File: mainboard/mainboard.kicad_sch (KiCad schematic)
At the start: 54 parts, among them J1 Servo, J2 ADC Pins, J3 USB Data, J4 Button Interface, J5 Power, J6 Release Button, J7 GPIO Pins, Q1 BSS138, SW1 SW_Push, U1 RP2040, U2 W25Q128JVS, U3 RV-3028-C7, U4 ITR9608-F, Y1 Crystal_ABM8

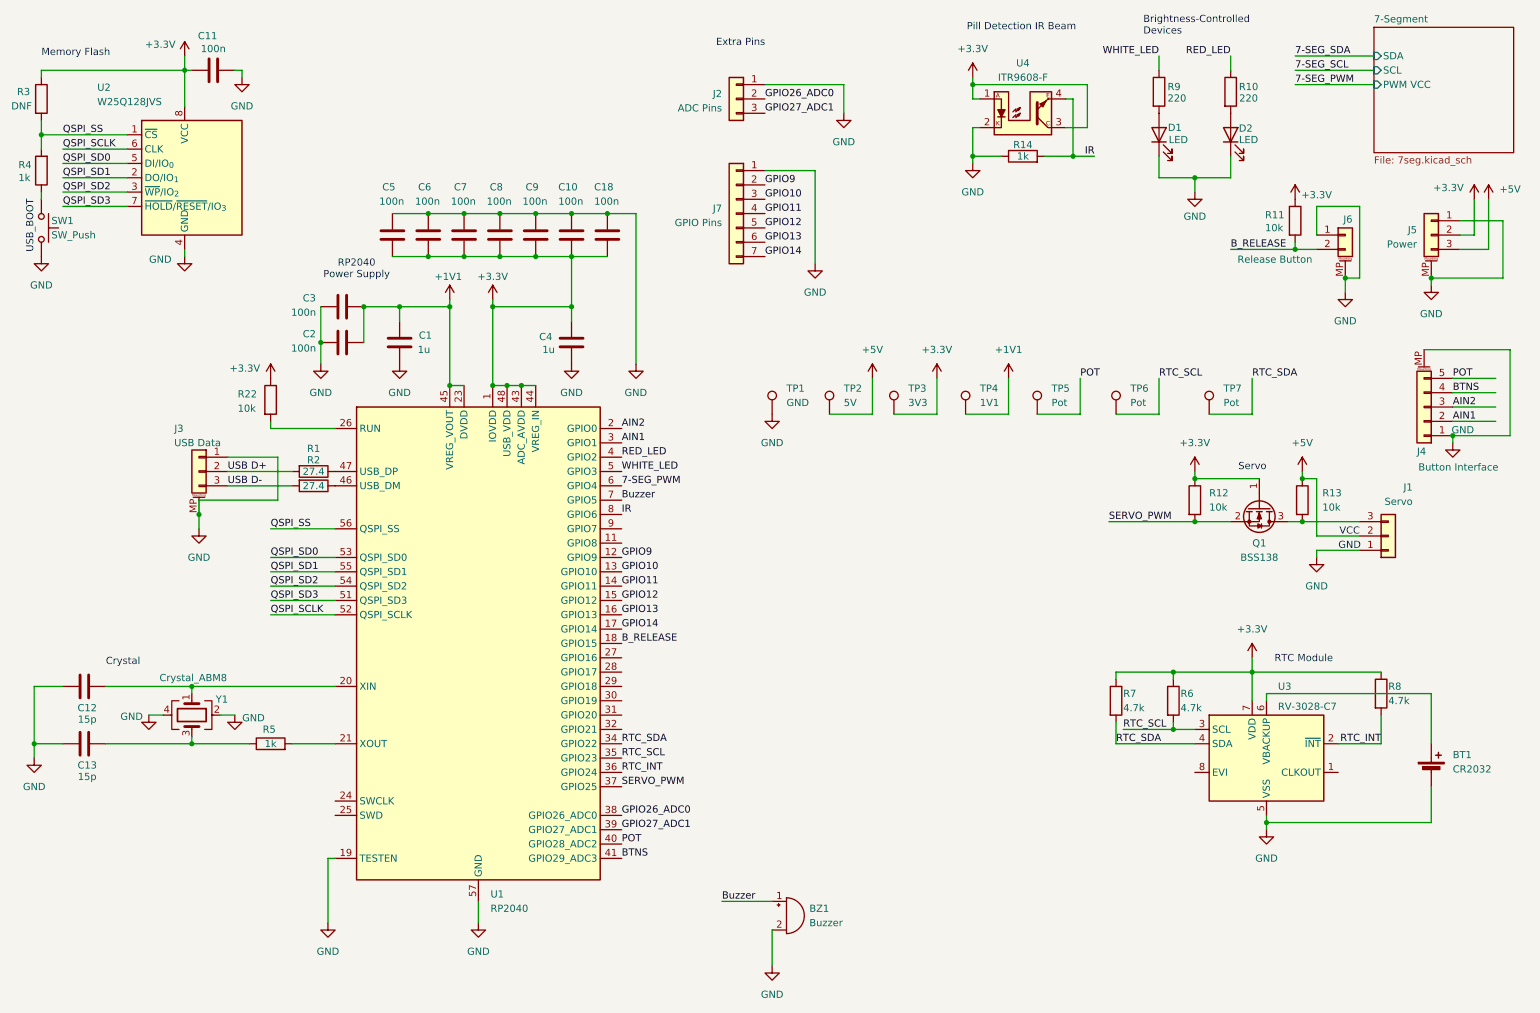
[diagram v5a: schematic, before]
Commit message: Replaced buzzer with connector, consolidated some connectors, rerouted traces.
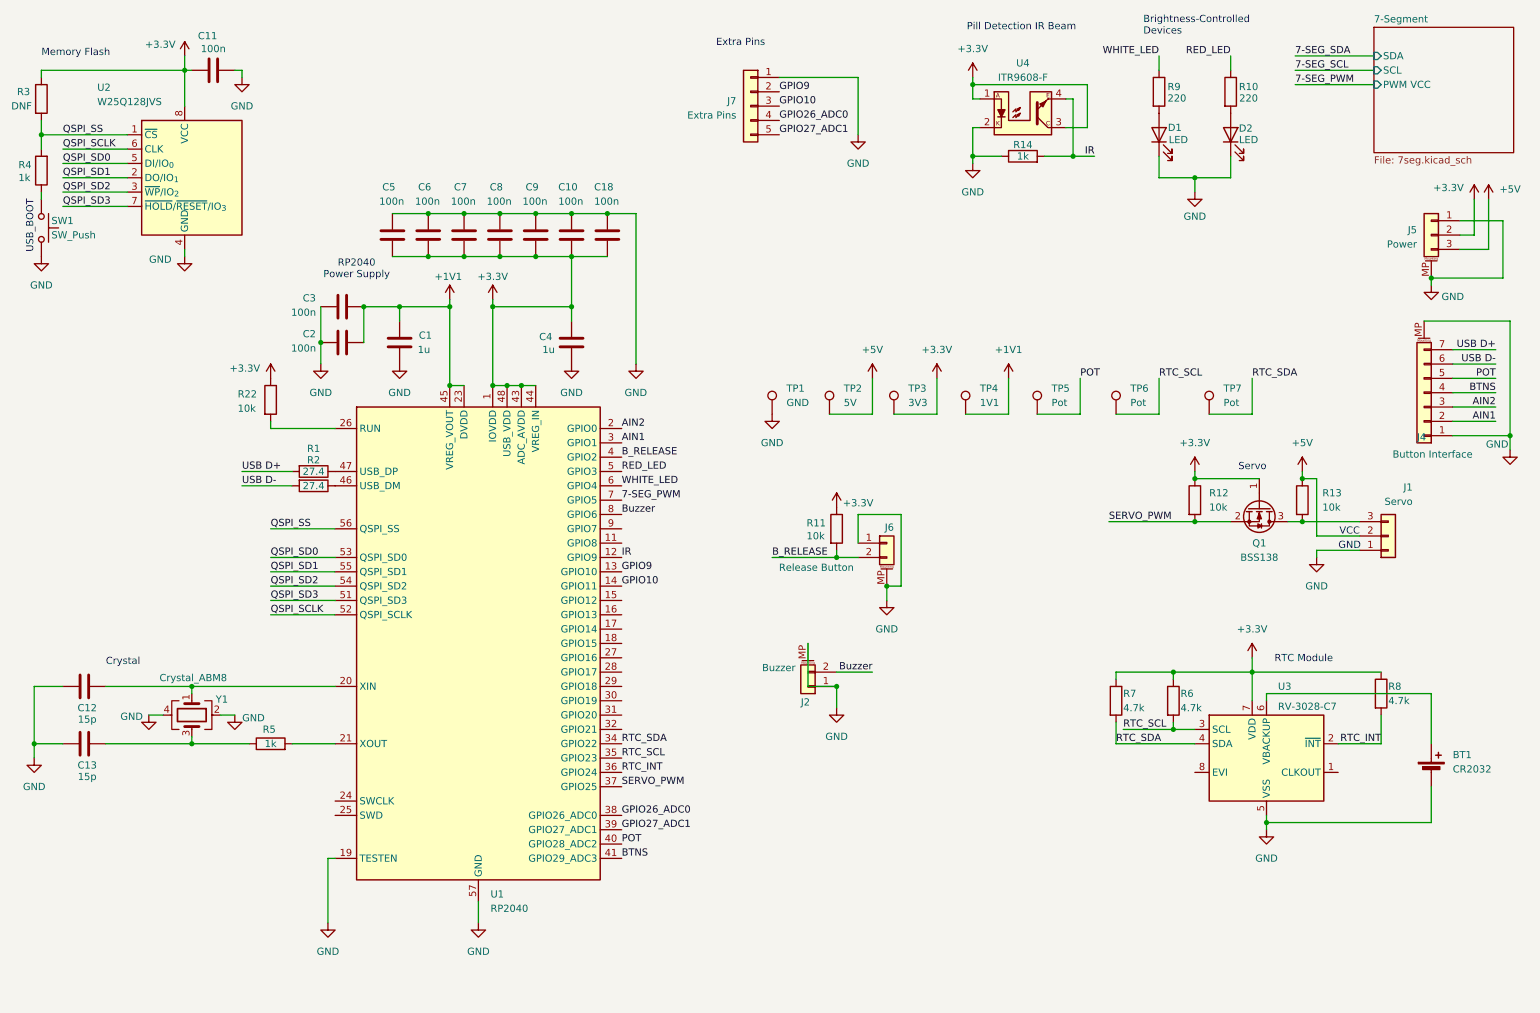
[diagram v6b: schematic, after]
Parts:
- removed BZ1: Buzzer, Buzzer_Beeper:Buzzer_12x9.5RM7.6, symbol Device:Buzzer
- removed J2: ADC Pins, Connector_PinHeader_2.54mm:PinHeader_1x03_P2.54mm_Vertical, symbol Connector_Generic:Conn_01x03
- removed J3: USB Data, Connector_Molex:Molex_CLIK-Mate_505405-0370_1x03-1MP_P1.50mm_Vertical, symbol Connector_Generic_MountingPin:Conn_01x03_MountingPin
- added J2: Buzzer, Connector_Molex:Molex_CLIK-Mate_505405-0270_1x02-1MP_P1.50mm_Vertical, symbol Connector_Generic_MountingPin:Conn_01x02_MountingPin
- D1, D2: footprint LED_THT:LED_D3.0mm -> LED_SMD:LED_1206_3216Metric
- J4: footprint Connector_Molex:Molex_CLIK-Mate_505405-0570_1x05-1MP_P1.50mm_Vertical -> Connector_Molex:Molex_CLIK-Mate_505405-0770_1x07-1MP_P1.50mm_Vertical; symbol Connector_Generic_MountingPin:Conn_01x05_MountingPin -> Connector_Generic_MountingPin:Conn_01x07_MountingPin
- J7: value GPIO Pins -> Extra Pins; footprint Connector_PinHeader_2.54mm:PinHeader_1x07_P2.54mm_Vertical -> Connector_PinHeader_2.54mm:PinHeader_1x05_P2.54mm_Vertical; symbol Connector_Generic:Conn_01x07 -> Connector_Generic:Conn_01x05
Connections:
- net 7-SEG_PWM: now also U1.7 (GPIO5); no longer U1.6 (GPIO4)
- net B_RELEASE: now also U1.4 (GPIO2); no longer U1.18 (GPIO15)
- net Buzzer: now also U1.8 (GPIO6), J2.2 (Pin_2); no longer U1.7 (GPIO5)
- net GND: now also J2.1 (Pin_1), J2.MP (MountPin)
- net GPIO10: now also U1.14 (GPIO11); no longer U1.13 (GPIO10)
- net GPIO26_ADC0: now also J7.4 (Pin_4)
- net GPIO27_ADC1: now also J7.5 (Pin_5)
- net GPIO9: now also U1.13 (GPIO10); no longer U1.12 (GPIO9)
- net IR: now also U1.12 (GPIO9); no longer U1.8 (GPIO6)
- net RED_LED: now also U1.5 (GPIO3); no longer U1.4 (GPIO2)
- net USB D+: now also J4.7 (Pin_7)
- net USB D-: now also J4.6 (Pin_6)
- net WHITE_LED: now also U1.6 (GPIO4); no longer U1.5 (GPIO3)
- removed net GPIO11: J7.4 (Pin_4), U1.14 (GPIO11)
- net GPIO12: no longer names the net of U1.15 (GPIO12)
- net GPIO12: no longer J7.5 (Pin_5)
- net GPIO13: no longer names the net of U1.16 (GPIO13)
- net GPIO13: no longer J7.6 (Pin_6)
- net GPIO14: no longer names the net of U1.17 (GPIO14)
- net GPIO14: no longer J7.7 (Pin_7)
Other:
- moved on the sheet: J6, R11

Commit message: trace management
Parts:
- TP6: value Pot -> SCL
- TP7: value Pot -> SDA
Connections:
- net USB D+: now also J4.6 (Pin_6); no longer J4.7 (Pin_7)
- net USB D-: now also J4.7 (Pin_7); no longer J4.6 (Pin_6)
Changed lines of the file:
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@@
 	)
 	(label "USB D-"
-		(at 279.4 76.2 180)
+		(at 279.4 73.66 180)
 		(effects
 			(font
@@
 	)
 	(label "USB D+"
-		(at 279.4 73.66 180)
+		(at 279.4 76.2 180)
 		(effects
 			(font
@@
 			)
 		)
-		(property "Value" "Pot"
+		(property "Value" "SCL"
 			(at 214.63 83.0579 0)
 			(effects
@@
 			)
 		)
-		(property "Value" "Pot"
+		(property "Value" "SDA"
 			(at 231.14 83.0579 0)
 			(effects

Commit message: Updated test points, moved mount points, & added some silkscreen stuff
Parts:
- TP1: footprint TestPoint:TestPoint_Pad_4.0x4.0mm -> TestPoint:TestPoint_THTPad_D1.0mm_Drill0.5mm
- TP2, TP3: footprint TestPoint:TestPoint_Pad_D2.0mm -> TestPoint:TestPoint_THTPad_D1.0mm_Drill0.5mm
- TP4, TP5, TP6, TP7: footprint TestPoint:TestPoint_Pad_D1.5mm -> TestPoint:TestPoint_THTPad_D1.0mm_Drill0.5mm
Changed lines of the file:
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@@
 			)
 		)
-		(property "Footprint" "TestPoint:TestPoint_Pad_D1.5mm"
+		(property "Footprint" "TestPoint:TestPoint_THTPad_D1.0mm_Drill0.5mm"
 			(at 217.17 85.09 0)
 			(effects
@@
 			)
 		)
-		(property "Footprint" "TestPoint:TestPoint_Pad_D1.5mm"
+		(property "Footprint" "TestPoint:TestPoint_THTPad_D1.0mm_Drill0.5mm"
 			(at 233.68 85.09 0)
 			(effects
@@
 			)
 		)
-		(property "Footprint" "TestPoint:TestPoint_Pad_4.0x4.0mm"
+		(property "Footprint" "TestPoint:TestPoint_THTPad_D1.0mm_Drill0.5mm"
 			(at 156.21 85.09 0)
 			(effects
@@
 			)
 		)
-		(property "Footprint" "TestPoint:TestPoint_Pad_D1.5mm"
+		(property "Footprint" "TestPoint:TestPoint_THTPad_D1.0mm_Drill0.5mm"
 			(at 203.2 85.09 0)
 			(effects
@@
 			)
 		)
-		(property "Footprint" "TestPoint:TestPoint_Pad_D2.0mm"
+		(property "Footprint" "TestPoint:TestPoint_THTPad_D1.0mm_Drill0.5mm"
 			(at 166.37 85.09 0)
 			(effects
@@
 			)
 		)
-		(property "Footprint" "TestPoint:TestPoint_Pad_D2.0mm"
+		(property "Footprint" "TestPoint:TestPoint_THTPad_D1.0mm_Drill0.5mm"
 			(at 177.8 85.09 0)
 			(effects
@@
 			)
 		)
-		(property "Footprint" "TestPoint:TestPoint_Pad_D1.5mm"
+		(property "Footprint" "TestPoint:TestPoint_THTPad_D1.0mm_Drill0.5mm"
 			(at 190.5 85.09 0)
 			(effects
